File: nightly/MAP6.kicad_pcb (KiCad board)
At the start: 2 copper layers, 49.9 x 74.9 mm, 35 parts, among them M1 Motor_vibration, P1 Logo_MA, P2 Pin, P3 LEG, P4 LEG, P5 LEG, P6 LEG, P7 LEG, P8 LEG, P9 STING, Q1 BC547, SW1 On, U1 LM555

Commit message: updated schematic and pcb
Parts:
- added kibuzzard-612E1065: G***, label, F.Cu at (148.5, 111.0)
- R1, R2: value 10E -> 150E
- R3: value 10E -> 15E
- R4, R6: footprint map6_fp:r_0805 -> map6_fp:r_0805_DNP
- kibuzzard-611CD92E: footprint label -> map6_fp:label_website
- kibuzzard-611CDC95 (x6): footprint label -> map6_fp:label_LEG
- kibuzzard-611CE09C: footprint label -> map6_fp:label_sting
- kibuzzard-611CF906: footprint label -> map6_fp:label_URL
- moved R3 5.00 mm to (148.5, 84.5)
- moved Q1 3.00 mm to (148.5, 92.0)
- moved M1 2.50 mm to (148.5, 102.5)
- moved R2 0.50 mm to (157.0, 88.0)
- moved kibuzzard-611CF906 0.40 mm to (132.0, 115.8)
- moved SW1 0.25 mm to (129.5, 113.5)
- moved R1 0.20 mm to (140.0, 88.0)
- renumbered P1 to G1, LOGO1 to G10, P2 to G2, P3 to G3, P4 to G4, P5 to G5, P6 to G6, P7 to G7, P8 to G8, P9 to G9
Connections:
- M1 pad 1: Net-(D1-Pad1) -> Net-(JP1-Pad2)
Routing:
- net /GND: track 388.2 -> 423.1 mm
- net Net-(D1-Pad1): track 49.6 -> 32.0 mm
- net Net-(JP1-Pad2): track 41.1 -> 52.0 mm
- net /motor: track 16.3 -> 19.5 mm
- net /6V: track 76.4 -> 78.6 mm
- net /right_eye: track 10.5 -> 10.0 mm
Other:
- net class 0.5 added: clearance 0.2, trace_width 0.5, via_dia 0.6, via_drill 0.4
- net class 1.0 added: clearance 0.2, trace_width 1, via_dia 0.6, via_drill 0.4
- net class Default added: clearance 0.2, trace_width 0.25, via_dia 0.6, via_drill 0.4

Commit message: big update, added several battery options
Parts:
- added BT2: BAT, map6_fp:cr2032_04_3025-2, B.Cu at (146.9, 111.5)
- BT1: footprint map6_fp:cr2032_02 -> map6_fp:cr2032_03
- M1: value Motor_vibration -> Motor
- R1, R2: value 150E -> 220E
- R3: value 15E -> 47E
- R4: value DNP -> 1k; footprint map6_fp:r_0805_DNP -> map6_fp:r_0805
- R6: value DNP -> 10k; footprint map6_fp:r_0805_DNP -> map6_fp:r_0805
- SW1: footprint map6_fp:SW_CuK_JS202011AQN_DPDT_Angled -> map6_fp:SW_SPDT_Straight
- moved kibuzzard-611CD92E 30.0 mm to (148.5, 96.5)
- moved R5 29.0 mm to (148.5, 87.5), turned to 180 degrees
- moved kibuzzard-611CF906 27.7 mm to (148.5, 93.5), turned to 180 degrees
- moved R4 14.1 mm to (138.5, 129.0), turned to 90 degrees
- moved M1 12.5 mm to (148.5, 90.0)
- moved C2 10.5 mm to (147.2, 136.5), turned to 0 degrees
- moved kibuzzard-611CDC95 10.3 mm to (166.5, 110.0)
- moved kibuzzard-611CDC95 10.3 mm to (130.5, 110.0)
- moved R6 8.90 mm to (141.5, 130.5), turned to 90 degrees
- moved Q1 8.00 mm to (148.5, 84.0)
- moved kibuzzard-611CDC95 7.25 mm to (164.5, 123.0)
- moved kibuzzard-611CDC95 7.25 mm to (132.5, 123.0)
- moved JP1 6.50 mm to (171.5, 117.0), turned to 90 degrees
- moved G7 6.40 mm to (133.5, 110.0)
- moved G8 6.40 mm to (163.5, 110.0)
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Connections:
- M1 pad 1: Net-(JP1-Pad2) -> Net-(D1-Pad1)
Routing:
- net /GND: track 423.1 -> 127.2 mm
- net Net-(R5-Pad2): track 40.5 -> 67.4 mm
- net Net-(BT1-Pad1): track 7.20 -> 32.2 mm
- net Net-(R4-Pad1): track 32.3 -> 12.4 mm
- net /6V: track 78.6 -> 90.9 mm
- net Net-(C1-Pad1): track 57.9 -> 51.4 mm
- net Net-(D1-Pad1): track 32.0 -> 29.1 mm
- net /right_eye: track 10.0 -> 8.58 mm
- net /left_eye: track 10.0 -> 8.58 mm
- net Net-(JP1-Pad2): track 52.0 -> 53.5 mm
- net Net-(C2-Pad1): track 6.78 -> 5.67 mm
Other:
- net class 0.5 removed
- net class 1.0 removed
- net class Default removed

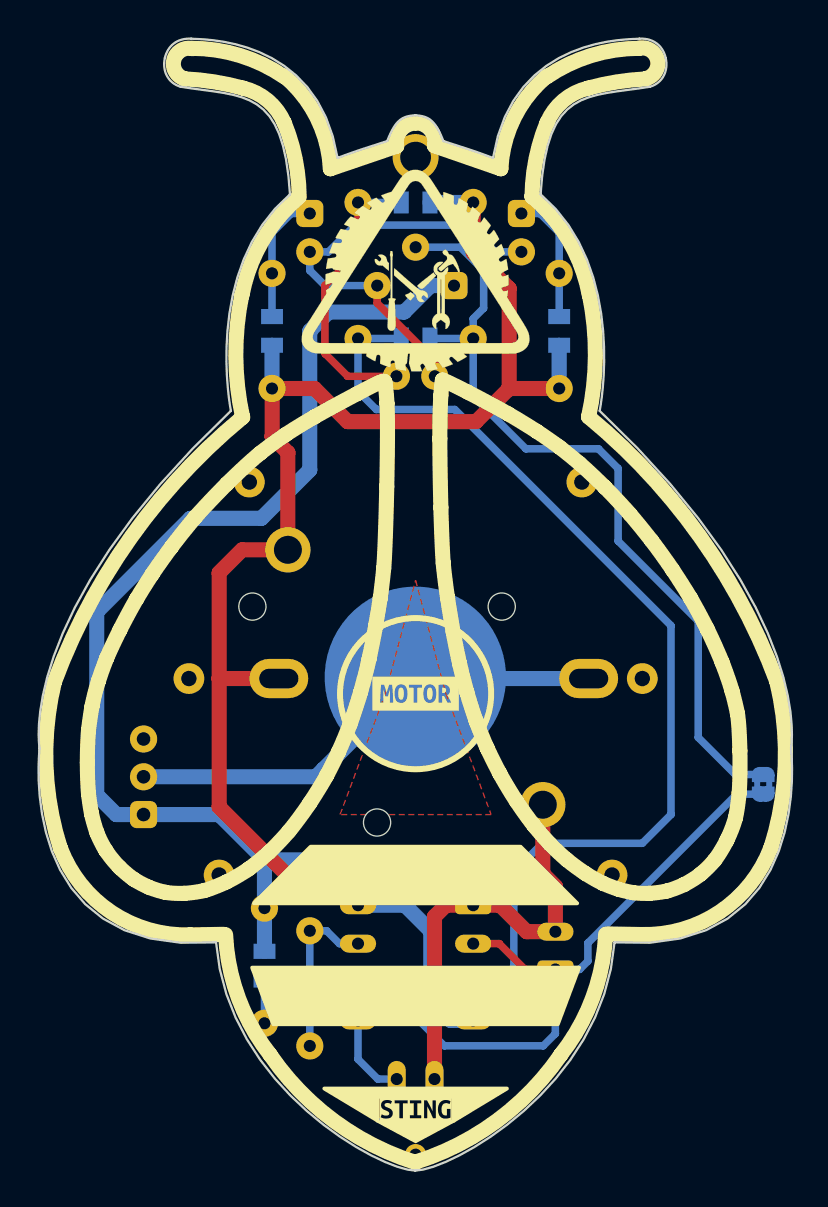
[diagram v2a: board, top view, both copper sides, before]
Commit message: another big update after deciding battery options. Ready for FAB
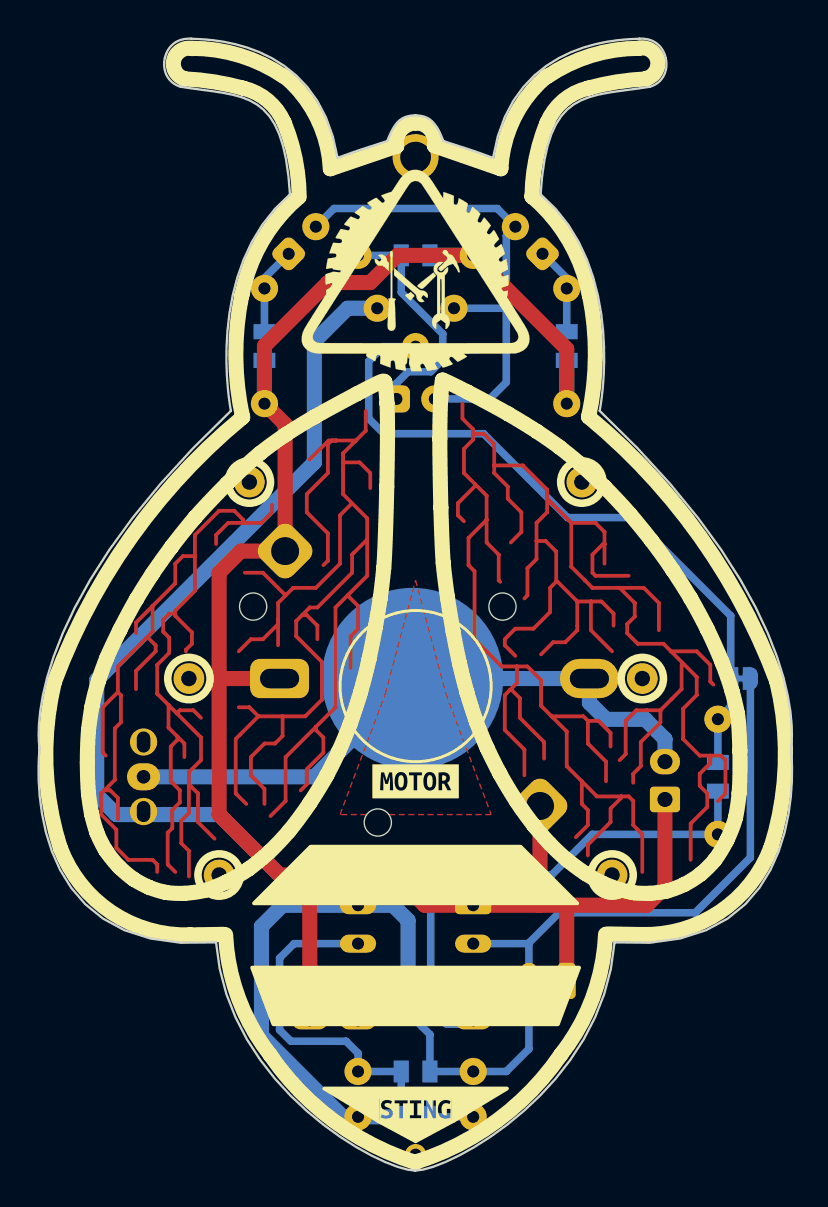
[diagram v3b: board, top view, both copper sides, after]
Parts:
- added J1: JST2, map6_fp:JST_EH_B2B-EH-A_1x02_P2.50mm_Vertical, B.Cu at (165.0, 118.0)
- moved R5 35.2 mm to (168.5, 116.5), turned to 270 degrees
- moved R1 19.5 mm to (158.5, 88.0)
- moved R2 19.5 mm to (138.5, 88.0)
- moved D1 14.5 mm to (156.0, 81.0), turned to 315 degrees
- moved D2 14.5 mm to (141.0, 81.0), turned to 225 degrees
- moved R4 14.1 mm to (148.5, 139.0), turned to 180 degrees
- moved G10 13.7 mm to (162.6, 101.1)
- moved R6 8.90 mm to (148.5, 136.0), turned to 180 degrees
- moved JP1 7.16 mm to (170.0, 110.0), turned to 180 degrees
- moved C2 6.94 mm to (141.5, 132.6), turned to 90 degrees
- moved kibuzzard-612E1065 5.80 mm to (148.5, 116.8)
- moved R3 3.50 mm to (148.5, 82.0)
- moved BT2 2.05 mm to (148.3, 110.0)
- moved C1 1.90 mm to (156.0, 130.0), turned to 0 degrees
- moved BT1 1.50 mm to (146.0, 110.0)
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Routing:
- net (no net): track 0.00 -> 408.4 mm
- net Net-(R5-Pad2): track 67.4 -> 31.8 mm
- net Net-(R4-Pad1): track 12.4 -> 27.6 mm
- net Net-(BT1-Pad1): track 32.2 -> 41.3 mm
- net Net-(JP1-Pad2): track 53.5 -> 46.7 mm
- net /GND: track 127.2 -> 133.3 mm
- net /6V: track 90.9 -> 96.2 mm
- net Net-(D1-Pad1): track 29.1 -> 33.4 mm
- net Net-(C1-Pad1): track 51.4 -> 55.4 mm
- net /motor: track 19.1 -> 15.6 mm
- net /right_eye: track 8.58 -> 5.82 mm
- net /left_eye: track 8.58 -> 5.82 mm
- net Net-(C2-Pad1): track 5.67 -> 3.19 mm
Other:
- net class 0.5 added: clearance 0.2, trace_width 0.5, via_dia 0.6, via_drill 0.4
- net class 1.0 added: clearance 0.2, trace_width 1, via_dia 0.6, via_drill 0.4
- net class Default added: clearance 0.2, trace_width 0.25, via_dia 0.6, via_drill 0.4
